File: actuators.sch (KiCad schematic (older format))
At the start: 35 parts, among them P1 VNLD5090e, P2 FAN1100, P3 VNLD5090e, P4 FAN1100, Q1 BTS3028SDL, Q2 BTS3028SDL, Q3 ISL9V3040, Q4 BTS3028SDL, Q5 ISL9V3040

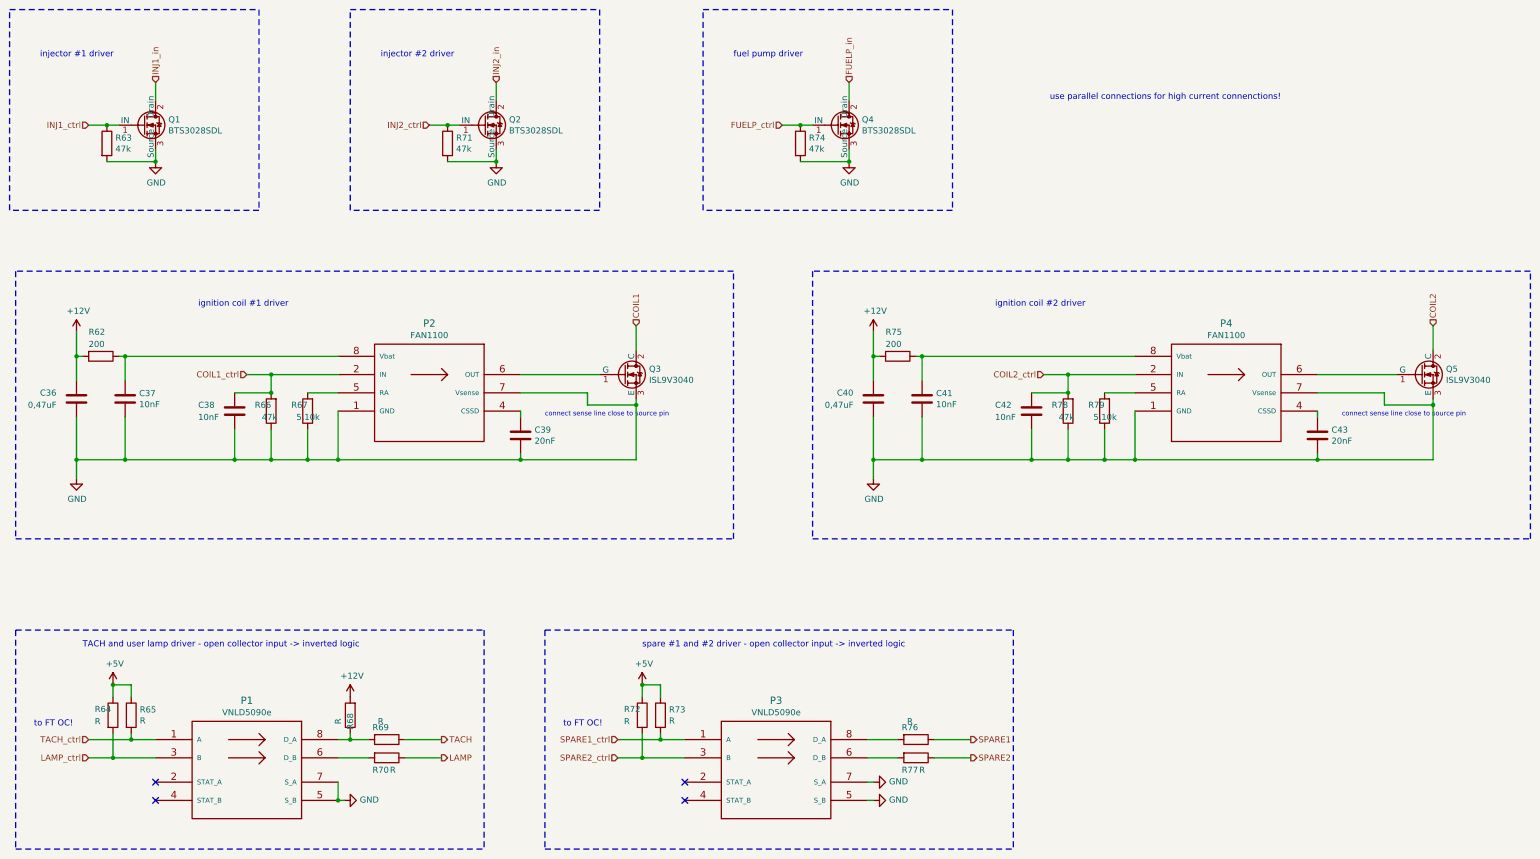
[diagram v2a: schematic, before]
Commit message: added missing component values working on BOM
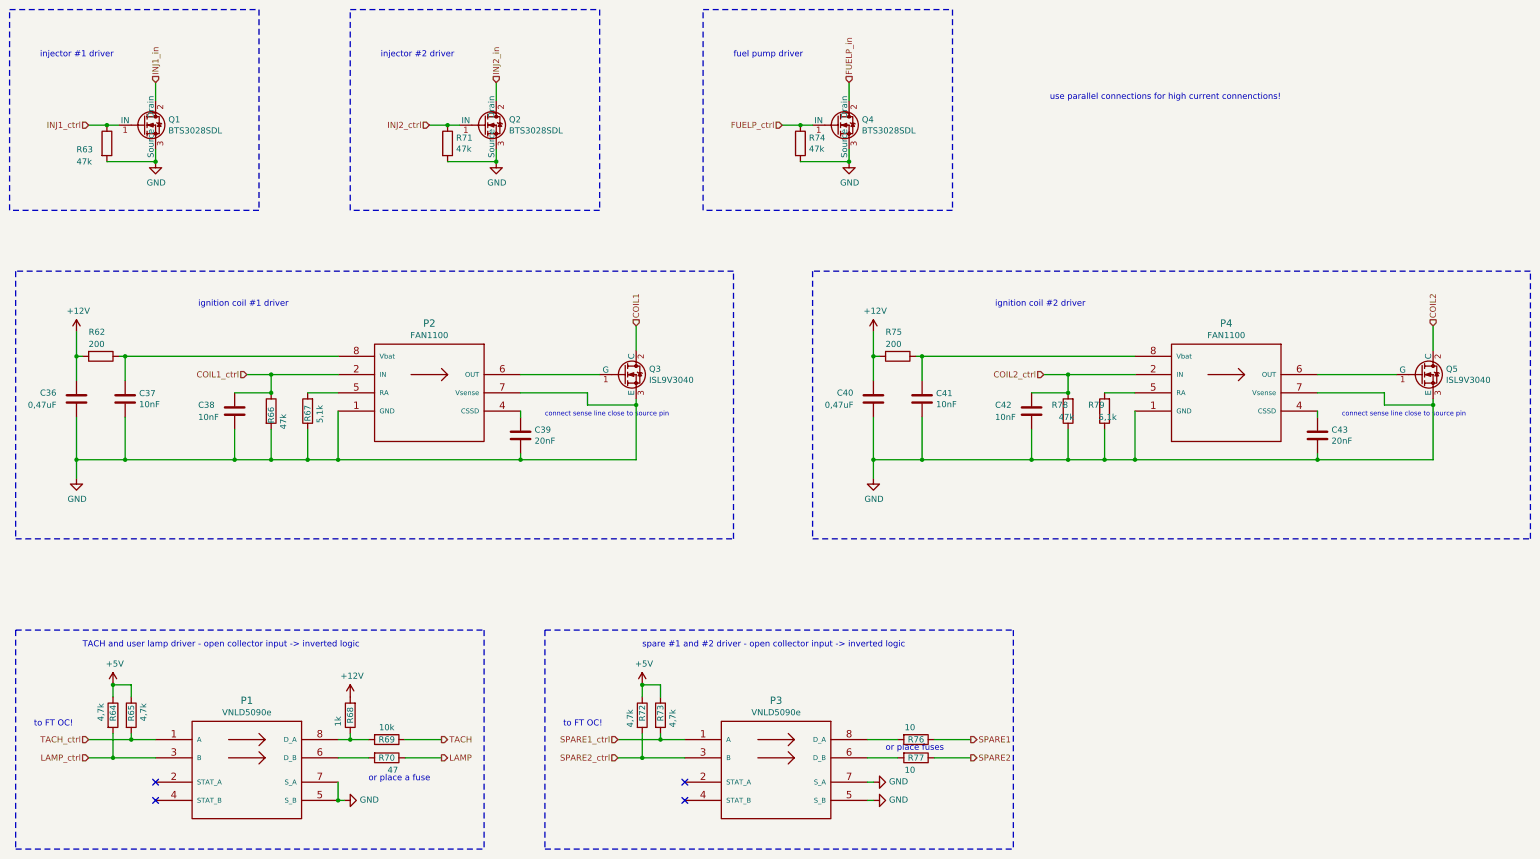
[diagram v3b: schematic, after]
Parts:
- C36, C40: Mouser (none) -> 80-C0805C474K5RECTU
- R64, R65, R72, R73: value R -> 4,7k
- R67, R79: value 5,10k -> 5,1k
- R68: value R -> 1k
- R69: value R -> 10k
- R70: value R -> 47
- R76, R77: value R -> 10
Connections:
- net COIL1_ctrl: now also R66.1; no longer R66.2
- net GND: now also R66.2; no longer R66.1
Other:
- note added: "or place a fuse"
- note added: "or place fuses"
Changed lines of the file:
@@
 U 1 1 5BD39757
 P 2100 2300
-F 0 "R63" H 2170 2346 50  0000 L CNN
-F 1 "47k" H 2170 2255 50  0000 L CNN
+F 0 "R63" H 1850 2250 50  0000 L CNN
+F 1 "47k" H 1850 2150 50  0000 L CNN
 F 2 "Resistor_SMD:R_0805_2012Metric" V 2030 2300 50  0001 C CNN
 F 3 "~" H 2100 2300 50  0001 C CNN
@@
 F 2 "Capacitor_SMD:C_0805_2012Metric" H 1888 4250 50  0001 C CNN
 F 3 "~" H 1850 4400 50  0001 C CNN
+F 4 "80-C0805C474K5RECTU" H 1850 4400 50  0001 C CNN "Mouser"
 	1    1850 4400
 	1    0    0    -1
@@
 U 1 1 5BDA6306
 P 2150 7000
-F 0 "R64" H 2000 7050 50  0000 L CNN
-F 1 "R" H 2000 6950 50  0000 L CNN
+F 0 "R64" V 2150 6950 50  0000 L CNN
+F 1 "4,7k" V 2050 6950 50  0000 L CNN
 F 2 "Resistor_SMD:R_0805_2012Metric" V 2080 7000 50  0001 C CNN
 F 3 "~" H 2150 7000 50  0001 C CNN
@@
 U 1 1 5BDA6378
 P 2300 7000
-F 0 "R65" H 2370 7046 50  0000 L CNN
-F 1 "R" H 2370 6955 50  0000 L CNN
+F 0 "R65" V 2300 6950 50  0000 L CNN
+F 1 "4,7k" V 2400 6950 50  0000 L CNN
 F 2 "Resistor_SMD:R_0805_2012Metric" V 2230 7000 50  0001 C CNN
 F 3 "~" H 2300 7000 50  0001 C CNN
@@
 U 1 1 5BDBAF8F
 P 4400 7200
-F 0 "R69" V 4300 7150 50  0000 C CNN
-F 1 "R" V 4250 7150 50  0000 C CNN
+F 0 "R69" V 4400 7200 50  0000 C CNN
+F 1 "10k" V 4300 7200 50  0000 C CNN
 F 2 "Resistor_SMD:R_0805_2012Metric" V 4330 7200 50  0001 C CNN
 F 3 "~" H 4400 7200 50  0001 C CNN
@@
 U 1 1 5BDBB004
 P 4400 7350
-F 0 "R70" V 4500 7300 50  0000 C CNN
-F 1 "R" V 4500 7400 50  0000 C CNN
+F 0 "R70" V 4400 7350 50  0000 C CNN
+F 1 "47" V 4500 7400 50  0000 C CNN
 F 2 "Resistor_SMD:R_0805_2012Metric" V 4330 7350 50  0001 C CNN
 F 3 "~" H 4400 7350 50  0001 C CNN
@@
 U 1 1 5BE45798
 P 3750 4500
-F 0 "R67" H 3750 4450 50  0000 L CNN
-F 1 "5,10k" H 3650 4550 50  0000 L CNN
+F 0 "R67" V 3750 4450 50  0000 L CNN
+F 1 "5,1k" V 3650 4450 50  0000 L CNN
 F 2 "Resistor_SMD:R_0805_2012Metric" V 3680 4500 50  0001 C CNN
 F 3 "~" H 3750 4500 50  0001 C CNN
@@
 U 1 1 5BE41142
 P 3450 4500
-F 0 "R66" H 3450 4450 50  0000 L CNN
-F 1 "47k" H 3400 4550 50  0000 L CNN
+F 0 "R66" V 3450 4400 50  0000 L CNN
+F 1 "47k" V 3550 4350 50  0000 L CNN
 F 2 "Resistor_SMD:R_0805_2012Metric" V 3380 4500 50  0001 C CNN
 F 3 "~" H 3450 4500 50  0001 C CNN
 	1    3450 4500
-	-1   0    0    1
+	1    0    0    -1
 $EndComp
 Wire Wire Line
@@
 F 2 "Capacitor_SMD:C_0805_2012Metric" H 8438 4250 50  0001 C CNN
 F 3 "~" H 8400 4400 50  0001 C CNN
+F 4 "80-C0805C474K5RECTU" H 8400 4400 50  0001 C CNN "Mouser"
 	1    8400 4400
 	1    0    0    -1
@@
 P 10300 4500
 F 0 "R79" H 10300 4450 50  0000 L CNN
-F 1 "5,10k" H 10200 4550 50  0000 L CNN
+F 1 "5,1k" H 10200 4550 50  0000 L CNN
 F 2 "Resistor_SMD:R_0805_2012Metric" V 10230 4500 50  0001 C CNN
 F 3 "~" H 10300 4500 50  0001 C CNN
@@
 U 1 1 5BEC26C6
 P 4100 7000
-F 0 "R68" V 4100 7050 50  0000 C CNN
-F 1 "R" V 4200 7050 50  0000 C CNN
+F 0 "R68" V 4100 7000 50  0000 C CNN
+F 1 "1k" V 4200 7050 50  0000 C CNN
 F 2 "Resistor_SMD:R_0805_2012Metric" V 4030 7000 50  0001 C CNN
 F 3 "~" H 4100 7000 50  0001 C CNN
@@
 U 1 1 5BEF0830
 P 6500 7000
-F 0 "R72" H 6350 7050 50  0000 L CNN
-F 1 "R" H 6350 6950 50  0000 L CNN
+F 0 "R72" V 6500 6950 50  0000 L CNN
+F 1 "4,7k" V 6400 6900 50  0000 L CNN
 F 2 "Resistor_SMD:R_0805_2012Metric" V 6430 7000 50  0001 C CNN
 F 3 "~" H 6500 7000 50  0001 C CNN
@@
 U 1 1 5BEF0836
 P 6650 7000
-F 0 "R73" H 6720 7046 50  0000 L CNN
-F 1 "R" H 6720 6955 50  0000 L CNN
+F 0 "R73" V 6650 6950 50  0000 L CNN
+F 1 "4,7k" V 6750 6900 50  0000 L CNN
 F 2 "Resistor_SMD:R_0805_2012Metric" V 6580 7000 50  0001 C CNN
 F 3 "~" H 6650 7000 50  0001 C CNN
@@
 U 1 1 5BEF085A
 P 8750 7200
-F 0 "R76" V 8650 7150 50  0000 C CNN
-F 1 "R" V 8600 7150 50  0000 C CNN
+F 0 "R76" V 8750 7200 50  0000 C CNN
+F 1 "10" V 8650 7150 50  0000 C CNN
 F 2 "Resistor_SMD:R_1210_3225Metric" V 8680 7200 50  0001 C CNN
 F 3 "~" H 8750 7200 50  0001 C CNN
@@
 U 1 1 5BEF0860
 P 8750 7350
-F 0 "R77" V 8850 7300 50  0000 C CNN
-F 1 "R" V 8850 7400 50  0000 C CNN
+F 0 "R77" V 8750 7350 50  0000 C CNN
+F 1 "10" V 8850 7300 50  0000 C CNN
 F 2 "Resistor_SMD:R_1210_3225Metric" V 8680 7350 50  0001 C CNN
 F 3 "~" H 8750 7350 50  0001 C CNN
@@
 Text Notes 9850 1950 0    50   ~ 0
 use parallel connections for high current connenctions!
+Text Notes 4250 7550 0    50   ~ 0
+or place a fuse
+Text Notes 8500 7300 0    50   ~ 0
+or place fuses
 $EndSCHEMATC

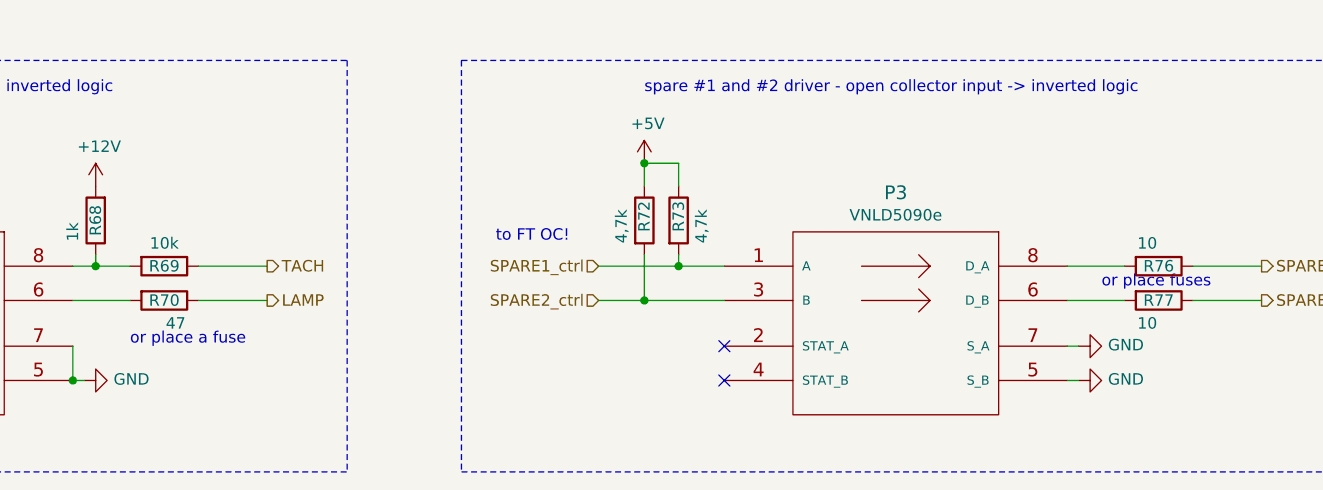
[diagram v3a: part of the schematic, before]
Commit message: cleaned BOMs
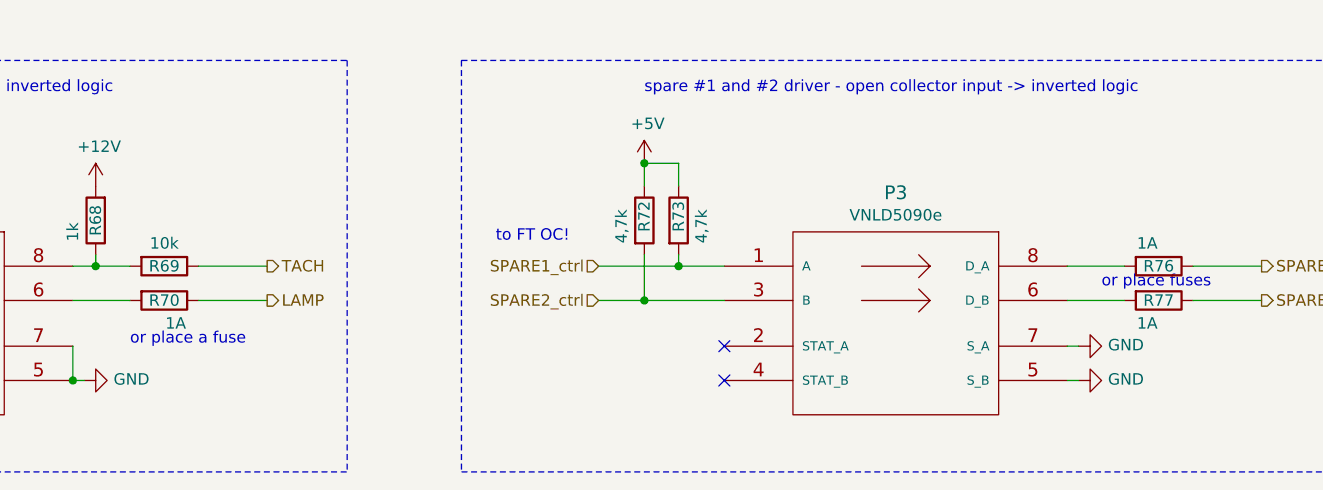
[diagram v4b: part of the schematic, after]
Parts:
- C37, C38, C41, C42: Mouser (none) -> 80-C0805C103K1R
- C39, C43: Mouser (none) -> 581-08055C203KAT2A
- P1, P3: Mouser (none) -> 511-VNLD5090-E
- P2, P4: Mouser (none) -> 512-FAN1100_F085
- Q1, Q2, Q4: Mouser (none) -> 726-BTS3028SDL
- Q3, Q5: Mouser (none) -> 512-ISL9V3040D3ST
- R62, R75: Mouser (none) -> 71-CRCW1206200RFKEAC
- R63, R66, R71, R74, R78: Mouser (none) -> 71-CRCW080547K0FKEAC
- R64, R65, R72, R73: Mouser (none) -> 71-CRCW08054K70FKEAC
- R67, R79: Mouser (none) -> 71-CRCW08055K10FKEAC
- R68: Mouser (none) -> 71-CRCW08051K00FKEAC
- R69: Mouser (none) -> 279-CRGCQ0805F10K
- R70: value 47 -> 1A; Mouser (none) -> 594-MFU0805-FF-1.0
- R76, R77: value 10 -> 1A; Mouser (none) -> 594-MFU1206FF01000P1
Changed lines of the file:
@@
 F 2 "Resistor_SMD:R_0805_2012Metric" V 2030 2300 50  0001 C CNN
 F 3 "~" H 2100 2300 50  0001 C CNN
+F 4 "71-CRCW080547K0FKEAC" H 2100 2300 50  0001 C CNN "Mouser"
 	1    2100 2300
 	1    0    0    -1
@@
 F 2 "Resistor_SMD:R_0805_2012Metric" V 4830 2300 50  0001 C CNN
 F 3 "~" H 4900 2300 50  0001 C CNN
+F 4 "71-CRCW080547K0FKEAC" H 4900 2300 50  0001 C CNN "Mouser"
 	1    4900 2300
 	1    0    0    -1
@@
 F 2 "Resistor_SMD:R_0805_2012Metric" V 7730 2300 50  0001 C CNN
 F 3 "~" H 7800 2300 50  0001 C CNN
+F 4 "71-CRCW080547K0FKEAC" H 7800 2300 50  0001 C CNN "Mouser"
 	1    7800 2300
 	1    0    0    -1
@@
 F 2 "Capacitor_SMD:C_0805_2012Metric" H 2288 4250 50  0001 C CNN
 F 3 "~" H 2250 4400 50  0001 C CNN
+F 4 "80-C0805C103K1R" H 2250 4400 50  0001 C CNN "Mouser"
 	1    2250 4400
 	1    0    0    -1
@@
 F 2 "Resistor_SMD:R_0805_2012Metric" V 2080 7000 50  0001 C CNN
 F 3 "~" H 2150 7000 50  0001 C CNN
+F 4 "71-CRCW08054K70FKEAC " H 2150 7000 50  0001 C CNN "Mouser"
 	1    2150 7000
 	1    0    0    -1
@@
 F 2 "Resistor_SMD:R_0805_2012Metric" V 2230 7000 50  0001 C CNN
 F 3 "~" H 2300 7000 50  0001 C CNN
+F 4 "71-CRCW08054K70FKEAC " H 2300 7000 50  0001 C CNN "Mouser"
 	1    2300 7000
 	1    0    0    -1
@@
 F 2 "Resistor_SMD:R_0805_2012Metric" V 4330 7200 50  0001 C CNN
 F 3 "~" H 4400 7200 50  0001 C CNN
+F 4 "279-CRGCQ0805F10K" H 4400 7200 50  0001 C CNN "Mouser"
 	1    4400 7200
 	0    1    1    0
@@
 P 4400 7350
 F 0 "R70" V 4400 7350 50  0000 C CNN
-F 1 "47" V 4500 7400 50  0000 C CNN
+F 1 "1A" V 4500 7400 50  0000 C CNN
 F 2 "Resistor_SMD:R_0805_2012Metric" V 4330 7350 50  0001 C CNN
 F 3 "~" H 4400 7350 50  0001 C CNN
+F 4 "594-MFU0805-FF-1.0" H 4400 7350 50  0001 C CNN "Mouser"
 	1    4400 7350
 	0    1    1    0
@@
 F 2 "boctok_footprints:FAN_1100" H 4850 4900 60  0001 C CNN
 F 3 "" H 4750 4350 60  0000 C CNN
+F 4 "512-FAN1100_F085" H 4750 4350 50  0001 C CNN "Mouser"
 	1    4750 4350
 	1    0    0    -1
@@
 F 2 "Resistor_SMD:R_1206_3216Metric" V 1980 4050 50  0001 C CNN
 F 3 "~" H 2050 4050 50  0001 C CNN
+F 4 "71-CRCW1206200RFKEAC" H 2050 4050 50  0001 C CNN "Mouser"
 	1    2050 4050
 	0    1    1    0
@@
 F 2 "Resistor_SMD:R_0805_2012Metric" V 3680 4500 50  0001 C CNN
 F 3 "~" H 3750 4500 50  0001 C CNN
+F 4 "71-CRCW08055K10FKEAC" H 3750 4500 50  0001 C CNN "Mouser"
 	1    3750 4500
 	-1   0    0    1
@@
 F 2 "Capacitor_SMD:C_0805_2012Metric" H 5538 4550 50  0001 C CNN
 F 3 "~" H 5500 4700 50  0001 C CNN
+F 4 "581-08055C203KAT2A " H 5500 4700 50  0001 C CNN "Mouser"
 	1    5500 4700
 	1    0    0    -1
@@
 F 2 "Resistor_SMD:R_0805_2012Metric" V 3380 4500 50  0001 C CNN
 F 3 "~" H 3450 4500 50  0001 C CNN
+F 4 "71-CRCW080547K0FKEAC" H 3450 4500 50  0001 C CNN "Mouser"
 	1    3450 4500
 	1    0    0    -1
@@
 F 2 "Capacitor_SMD:C_0805_2012Metric" H 3188 4350 50  0001 C CNN
 F 3 "~" H 3150 4500 50  0001 C CNN
+F 4 "80-C0805C103K1R" H 3150 4500 50  0001 C CNN "Mouser"
 	1    3150 4500
 	1    0    0    -1
@@
 F 2 "Capacitor_SMD:C_0805_2012Metric" H 8838 4250 50  0001 C CNN
 F 3 "~" H 8800 4400 50  0001 C CNN
+F 4 "80-C0805C103K1R" H 8800 4400 50  0001 C CNN "Mouser"
 	1    8800 4400
 	1    0    0    -1
@@
 F 2 "boctok_footprints:FAN_1100" H 11400 4900 60  0001 C CNN
 F 3 "" H 11300 4350 60  0000 C CNN
+F 4 "512-FAN1100_F085" H 11300 4350 50  0001 C CNN "Mouser"
 	1    11300 4350
 	1    0    0    -1
@@
 F 2 "Resistor_SMD:R_1206_3216Metric" V 8530 4050 50  0001 C CNN
 F 3 "~" H 8600 4050 50  0001 C CNN
+F 4 "71-CRCW1206200RFKEAC" H 8600 4050 50  0001 C CNN "Mouser"
 	1    8600 4050
 	0    1    1    0
@@
 F 2 "Resistor_SMD:R_0805_2012Metric" V 10230 4500 50  0001 C CNN
 F 3 "~" H 10300 4500 50  0001 C CNN
+F 4 "71-CRCW08055K10FKEAC" H 10300 4500 50  0001 C CNN "Mouser"
 	1    10300 4500
 	-1   0    0    1
@@
 F 2 "Capacitor_SMD:C_0805_2012Metric" H 12088 4550 50  0001 C CNN
 F 3 "~" H 12050 4700 50  0001 C CNN
+F 4 "581-08055C203KAT2A " H 12050 4700 50  0001 C CNN "Mouser"
 	1    12050 4700
 	1    0    0    -1
@@
 F 2 "Resistor_SMD:R_0805_2012Metric" V 9930 4500 50  0001 C CNN
 F 3 "~" H 10000 4500 50  0001 C CNN
+F 4 "71-CRCW080547K0FKEAC" H 10000 4500 50  0001 C CNN "Mouser"
 	1    10000 4500
 	-1   0    0    1
@@
 F 2 "Capacitor_SMD:C_0805_2012Metric" H 9738 4350 50  0001 C CNN
 F 3 "~" H 9700 4500 50  0001 C CNN
+F 4 "80-C0805C103K1R" H 9700 4500 50  0001 C CNN "Mouser"
 	1    9700 4500
 	1    0    0    -1
@@
 F 2 "boctok_footprints:VNLD5090e" H 3350 8000 60  0001 C CNN
 F 3 "" H 3250 7550 60  0000 C CNN
+F 4 "511-VNLD5090-E" H 3250 7450 50  0001 C CNN "Mouser"
 	1    3250 7450
 	1    0    0    -1
@@
 F 2 "Resistor_SMD:R_0805_2012Metric" V 4030 7000 50  0001 C CNN
 F 3 "~" H 4100 7000 50  0001 C CNN
+F 4 "71-CRCW08051K00FKEAC " H 4100 7000 50  0001 C CNN "Mouser"
 	1    4100 7000
 	-1   0    0    1
@@
 F 2 "Resistor_SMD:R_0805_2012Metric" V 6430 7000 50  0001 C CNN
 F 3 "~" H 6500 7000 50  0001 C CNN
+F 4 "71-CRCW08054K70FKEAC " H 6500 7000 50  0001 C CNN "Mouser"
 	1    6500 7000
 	1    0    0    -1
@@
 F 2 "Resistor_SMD:R_0805_2012Metric" V 6580 7000 50  0001 C CNN
 F 3 "~" H 6650 7000 50  0001 C CNN
+F 4 "71-CRCW08054K70FKEAC " H 6650 7000 50  0001 C CNN "Mouser"
 	1    6650 7000
 	1    0    0    -1
@@
 P 8750 7200
 F 0 "R76" V 8750 7200 50  0000 C CNN
-F 1 "10" V 8650 7150 50  0000 C CNN
+F 1 "1A" V 8650 7150 50  0000 C CNN
 F 2 "Resistor_SMD:R_1210_3225Metric" V 8680 7200 50  0001 C CNN
 F 3 "~" H 8750 7200 50  0001 C CNN
+F 4 "594-MFU1206FF01000P1 " H 8750 7200 50  0001 C CNN "Mouser"
 	1    8750 7200
 	0    1    1    0
@@
 P 8750 7350
 F 0 "R77" V 8750 7350 50  0000 C CNN
-F 1 "10" V 8850 7300 50  0000 C CNN
+F 1 "1A" V 8850 7300 50  0000 C CNN
 F 2 "Resistor_SMD:R_1210_3225Metric" V 8680 7350 50  0001 C CNN
 F 3 "~" H 8750 7350 50  0001 C CNN
+F 4 "594-MFU1206FF01000P1 " H 8750 7350 50  0001 C CNN "Mouser"
 	1    8750 7350
 	0    1    1    0
@@
 F 2 "boctok_footprints:VNLD5090e" H 7700 8000 60  0001 C CNN
 F 3 "" H 7600 7550 60  0000 C CNN
+F 4 "511-VNLD5090-E" H 7600 7450 50  0001 C CNN "Mouser"
 	1    7600 7450
 	1    0    0    -1
@@
 F 2 "boctok_footprints:BTS3028SD" H 2600 2075 50  0001 L CIN
 F 3 "" H 2400 2150 50  0001 L CNN
+F 4 "726-BTS3028SDL" H 2400 2150 50  0001 C CNN "Mouser"
 	1    2400 2150
 	1    0    0    -1
@@
 F 2 "boctok_footprints:BTS3028SD" H 5400 2075 50  0001 L CIN
 F 3 "" H 5200 2150 50  0001 L CNN
+F 4 "726-BTS3028SDL" H 5200 2150 50  0001 C CNN "Mouser"
 	1    5200 2150
 	1    0    0    -1
@@
 F 2 "boctok_footprints:BTS3028SD" H 8300 2075 50  0001 L CIN
 F 3 "" H 8100 2150 50  0001 L CNN
+F 4 "726-BTS3028SDL" H 8100 2150 50  0001 C CNN "Mouser"
 	1    8100 2150
 	1    0    0    -1
@@
 F 2 "boctok_footprints:ISL9V3040" H 6550 4125 50  0001 L CIN
 F 3 "" H 6350 4200 50  0001 L CNN
+F 4 "512-ISL9V3040D3ST" H 6350 4200 50  0001 C CNN "Mouser"
 	1    6350 4200
 	1    0    0    -1
@@
 F 2 "boctok_footprints:ISL9V3040" H 13100 4125 50  0001 L CIN
 F 3 "" H 12900 4200 50  0001 L CNN
+F 4 "512-ISL9V3040D3ST" H 12900 4200 50  0001 C CNN "Mouser"
 	1    12900 4200
 	1    0    0    -1
